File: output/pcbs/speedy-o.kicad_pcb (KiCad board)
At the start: 2 copper layers, 172 x 125.7 mm, 60 parts

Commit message: submit old config
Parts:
- added ?: , HOLE_M2_TH, F.Cu at (135.4, 138.9)
- added ?: , HOLE_M2_TH, F.Cu at (198.4, 141.4)
- added ?: , HOLE_M2_TH, F.Cu at (244.4, 136.3)
- added ?: , HOLE_M2_TH, F.Cu at (105.4, 74.9)
- added ?: , HOLE_M2_TH, F.Cu at (200.4, 57.5)
- added ?: , HOLE_M2_TH, F.Cu at (244.4, 79.3)
- added JST1: , JST_PH_S2B-PH-K_02x2.00mm_Angled, F.Cu at (206.6, 77.4)
- added LED1: , WS2812B,  at (100.9, 154.9)
- added LED10: , WS2812B,  at (135.4, 112.2)
- added LED11: , WS2812B,  at (135.4, 93.2)
- added LED12: , WS2812B,  at (135.4, 74.2)
- added LED13: , WS2812B,  at (154.4, 125.2)
- added LED14: , WS2812B,  at (154.4, 106.2)
- added LED15: , WS2812B,  at (154.4, 87.2)
- added LED16: , WS2812B,  at (154.4, 68.2)
- added LED17: , WS2812B,  at (173.4, 130.9)
- added LED18: , WS2812B,  at (173.4, 111.9)
- added LED19: , WS2812B,  at (173.4, 92.9)
- added LED2: , WS2812B,  at (97.6, 136.2)
- added LED20: , WS2812B,  at (173.4, 73.9)
- added LED21: , WS2812B,  at (192.4, 133.7)
- added LED22: , WS2812B,  at (192.4, 114.7)
- added LED23: , WS2812B,  at (192.4, 95.7)
- added LED24: , WS2812B,  at (192.4, 76.7)
- added LED25: , WS2812B,  at (182.0, 154.7)
- added LED26: , WS2812B,  at (206.5, 160.9)
- added LED27: , WS2812B,  at (213.0, 143.1)
- added LED28: , WS2812B,  at (223.8, 169.3)
- added LED29: , WS2812B,  at (233.3, 152.8)
- added LED3: , WS2812B,  at (94.3, 117.5)
- added LED4: , WS2812B,  at (91.0, 98.8)
- added LED5: , WS2812B,  at (119.6, 151.6)
- added LED6: , WS2812B,  at (116.3, 132.9)
- added LED7: , WS2812B,  at (113.0, 114.2)
- added LED8: , WS2812B,  at (109.7, 95.5)
- added LED9: , WS2812B,  at (135.4, 131.2)
- added TRRS1: TRRS-PJ-320A-dual, TRRS-PJ-320A-dual, F.Cu at (238.4, 73.6)
- D1, D10, D11, D12, D13, D14, D15, D16, D17, D18, D19, D2, D20, D21, D22, D23, D24, D25, D26, D27, D28, D29, D3, D4, D5, D6, D7, D8, D9: value (none) -> Nexperia_CFP3_SOD-123W; footprint ComboDiode -> Diode_SMD:Nexperia_CFP3_SOD-123W; moved to 
- moved D1 11.2 mm to (91.7, 148.4), turned to 100 degrees
- moved D2 11.2 mm to (88.4, 129.7), turned to 100 degrees
- moved D3 11.2 mm to (85.1, 111.0), turned to 100 degrees
- moved D4 11.2 mm to (81.8, 92.3), turned to 100 degrees
- moved D5 11.2 mm to (110.4, 145.1), turned to 100 degrees
- moved D6 11.2 mm to (107.1, 126.4), turned to 100 degrees
- moved D7 11.2 mm to (103.8, 107.7), turned to 100 degrees
- moved D8 11.2 mm to (100.5, 89.0), turned to 100 degrees
- moved D25 11.2 mm to (175.7, 145.4), turned to 80 degrees
- moved D26 11.2 mm to (201.8, 150.7), turned to 70 degrees
- moved D27 11.2 mm to (208.3, 132.8), turned to 70 degrees
- moved D17 11.2 mm to (165.5, 122.9), turned to 90 degrees
- moved D10 11.2 mm to (127.5, 104.2), turned to 90 degrees
- moved D11 11.2 mm to (127.5, 85.2), turned to 90 degrees
- moved D12 11.2 mm to (127.5, 66.2), turned to 90 degrees
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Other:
- board text added: "Speedy-O"

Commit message: update config
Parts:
- removed the ? at (135.4, 138.9)
- removed the ? at (198.4, 141.4)
- removed the ? at (244.4, 136.3)
- removed the ? at (105.4, 74.9)
- removed the ? at (200.4, 57.5)
- removed the ? at (244.4, 79.3)
- removed D28, D29: Nexperia_CFP3_SOD-123W, Diode_SMD:Nexperia_CFP3_SOD-123W
- removed JST1: , JST_PH_S2B-PH-K_02x2.00mm_Angled
- removed LED28, LED29: , WS2812B
- removed MCU1: nice_nano, nice_nano
- removed S28, S29: , PG1350
- added ?: , ProMicro, F.Cu at (207.4, 90.0)
- added T1: , Button_Switch_SMD:SW_SPDT_PCM12, F.Cu at (218.9, 128.0)
- added _2: , Connector_JST:JST_PH_S2B-PH-K_1x02_P2.00mm_Horizontal,  at (209.4, 116.0)
- added _3: , MountingHole_2.2mm_M2_Pad_Via, F.Cu at (120.0, 78.0)
- added _4: , MountingHole_2.2mm_M2_Pad_Via, F.Cu at (134.4, 146.0)
- added _5: , MountingHole_2.2mm_M2_Pad_Via, F.Cu at (170.4, 146.0)
- added _6: , MountingHole_2.2mm_M2_Pad_Via, F.Cu at (213.7, 135.0)
- added _7: , MountingHole_2.2mm_M2_Pad_Via, F.Cu at (220.8, 97.0)
- moved D27 26.8 mm to (219.3, 157.2), turned to 54 degrees
- moved S27 25.0 mm to (226.4, 160.4), turned to -36 degrees
- moved LED27 23.8 mm to (223.5, 164.5), turned to -36 degrees
- moved D16 17.4 mm to (144.8, 77.6)
- moved TRRS1 16.5 mm to (221.9, 74.2)
- moved D15 15.5 mm to (144.8, 94.6)
- moved D20 14.0 mm to (162.8, 79.6)
- moved D14 13.5 mm to (144.8, 111.6)
- moved D24 13.4 mm to (180.8, 81.6)
- moved D12 13.4 mm to (126.8, 79.6)
- moved LED16 12.9 mm to (152.4, 81.0)
- moved S16 12.9 mm to (152.4, 76.0)
- moved D19 12.0 mm to (162.8, 96.6)
- moved D13 11.5 mm to (144.8, 128.6)
- moved D23 11.5 mm to (180.8, 98.6)
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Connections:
- net P006 renamed P10
- net P008 renamed P9
- net P011 renamed P2
- net P017 renamed P8
- net P100 renamed P1
- net P104 renamed P3
- net P106 renamed P4
- net first_home renamed thumb_inner_home
- net index_bottom renamed main_index_bottom
- net index_home renamed main_index_home
- net index_num renamed main_index_num
- net index_top renamed main_index_top
- net inner_bottom renamed main_inner_bottom
- net inner_home renamed main_inner_home
- net inner_num renamed main_inner_num
- net inner_top renamed main_inner_top
- net middle_bottom renamed main_middle_bottom
- net middle_home renamed main_middle_home
- net middle_num renamed main_middle_num
- net middle_top renamed main_middle_top
- net outer_bottom renamed main_outer_bottom
- net outer_home renamed main_outer_home
- net outer_num renamed main_outer_num
- net outer_top renamed main_outer_top
- net pinky_bottom renamed main_pinky_bottom
- net pinky_home renamed main_pinky_home
- net pinky_num renamed main_pinky_num
- net pinky_top renamed main_pinky_top
- net ring_bottom renamed main_ring_bottom
- net ring_home renamed main_ring_home
- net ring_num renamed main_ring_num
- net ring_top renamed main_ring_top
- net second_home renamed thumb_home_home
- net second_upper renamed thumb_outer_home
- D25 pad 1: (no net) -> P11
- D26 pad 1: (no net) -> P11
- D27 pad 1: (no net) -> P11
- LED1 pad 4: (no net) -> rgb_main_outer_bottom
- LED10 pad 2: (no net) -> rgb_main_ring_bottom
- LED10 pad 4: (no net) -> rgb_main_ring_home
- LED11 pad 2: (no net) -> rgb_main_ring_home
- LED11 pad 4: (no net) -> rgb_main_ring_top
- LED12 pad 2: (no net) -> rgb_main_ring_top
- LED12 pad 4: (no net) -> rgb_main_ring_num
- LED13 pad 2: (no net) -> rgb_main_middle_home
- LED13 pad 4: (no net) -> rgb_main_middle_bottom
- LED14 pad 2: (no net) -> rgb_main_middle_top
- LED14 pad 4: (no net) -> rgb_main_middle_home
- LED15 pad 2: (no net) -> rgb_main_middle_num
- LED15 pad 4: (no net) -> rgb_main_middle_top
- LED16 pad 2: (no net) -> rgb_main_ring_num
- LED16 pad 4: (no net) -> rgb_main_middle_num
- LED17 pad 2: (no net) -> rgb_thumb_home_home
- LED17 pad 4: (no net) -> rgb_main_index_bottom
- LED18 pad 2: (no net) -> rgb_main_index_bottom
- LED18 pad 4: (no net) -> rgb_main_index_home
- LED19 pad 2: (no net) -> rgb_main_index_home
- LED19 pad 4: (no net) -> rgb_main_index_top
- LED2 pad 2: (no net) -> rgb_main_outer_bottom
- LED2 pad 4: (no net) -> rgb_main_outer_home
- LED20 pad 2: (no net) -> rgb_main_index_top
- LED20 pad 4: (no net) -> rgb_main_index_num
- LED21 pad 2: (no net) -> rgb_main_inner_home
- LED21 pad 4: (no net) -> rgb_main_inner_bottom
- LED22 pad 2: (no net) -> rgb_main_inner_top
- LED22 pad 4: (no net) -> rgb_main_inner_home
- LED23 pad 2: (no net) -> rgb_main_inner_num
- LED23 pad 4: (no net) -> rgb_main_inner_top
- LED24 pad 2: (no net) -> rgb_main_index_num
- LED24 pad 4: (no net) -> rgb_main_inner_num
- LED25 pad 2: (no net) -> rgb_main_middle_bottom
- LED25 pad 4: (no net) -> rgb_thumb_inner_home
- LED26 pad 2: (no net) -> rgb_thumb_inner_home
- LED26 pad 4: (no net) -> rgb_thumb_home_home
- LED27 pad 2: (no net) -> rgb_main_inner_bottom
- LED27 pad 4: (no net) -> P12
- LED3 pad 2: (no net) -> rgb_main_outer_home
- LED3 pad 4: (no net) -> rgb_main_outer_top
- LED4 pad 2: (no net) -> rgb_main_outer_top
- LED4 pad 4: (no net) -> rgb_main_outer_num
- LED5 pad 2: (no net) -> rgb_main_pinky_home
- LED5 pad 4: (no net) -> rgb_main_pinky_bottom
- LED6 pad 2: (no net) -> rgb_main_pinky_top
- LED6 pad 4: (no net) -> rgb_main_pinky_home
- LED7 pad 2: (no net) -> rgb_main_pinky_num
- LED7 pad 4: (no net) -> rgb_main_pinky_top
- LED8 pad 2: (no net) -> rgb_main_outer_num
- LED8 pad 4: (no net) -> rgb_main_pinky_num
- LED9 pad 2: (no net) -> rgb_main_pinky_bottom
- LED9 pad 4: (no net) -> rgb_main_ring_bottom
- S13 pad 1: P020 -> P7
- S14 pad 1: P020 -> P7
- S15 pad 1: P020 -> P7
- S16 pad 1: P020 -> P7
- S17 pad 1: P022 -> P6
- S18 pad 1: P022 -> P6
- S19 pad 1: P022 -> P6
- S20 pad 1: P022 -> P6
- S21 pad 1: P024 -> P5
- S22 pad 1: P024 -> P5
- S23 pad 1: P024 -> P5
- S24 pad 1: P024 -> P5
- S25 pad 1: P009 -> P5
- S26 pad 1: P010 -> P6
- S27 pad 1: P111 -> P7
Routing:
- net (no net): track 0.00 -> 371.4 mm
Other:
- board size 172 x 125.7 mm -> 159.3 x 108.6 mm
- board text added: "Speedy-O v0.1.0"
- board text removed: "Speedy-O"

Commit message: alternative layout
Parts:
- moved TRRS1 46.7 mm to (218.1, 120.8), turned to -90 degrees
- moved _2 10.2 mm to (199.2, 116.0), turned to 180 degrees
- moved T1 2.24 mm to (216.7, 128.0)
- moved ? 1.00 mm to (208.4, 90.0)
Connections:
- D25 pad 1: P11 -> P8
- D25 pad 2: thumb_inner_home -> thumb_outer_home
- D26 pad 1: P11 -> P8
- D27 pad 1: P11 -> P8
- D27 pad 2: thumb_outer_home -> thumb_inner_home
- LED25 pad 4: rgb_thumb_inner_home -> rgb_thumb_outer_home
- LED27 pad 4: P12 -> P9
- S25 pad 2: thumb_inner_home -> thumb_outer_home
- S26 pad 1: P6 -> P4
- S27 pad 1: P7 -> P3
- S27 pad 2: thumb_outer_home -> thumb_inner_home
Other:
- outline, holes or cut-outs redrawn

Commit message: update routing
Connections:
- D1 pad 1: P1 -> P6
- D10 pad 1: P2 -> P7
- D11 pad 1: P3 -> P8
- D12 pad 1: P4 -> P9
- D13 pad 1: P1 -> P6
- D14 pad 1: P2 -> P7
- D15 pad 1: P3 -> P8
- D16 pad 1: P4 -> P9
- D17 pad 1: P1 -> P6
- D18 pad 1: P2 -> P7
- D19 pad 1: P3 -> P8
- D2 pad 1: P2 -> P7
- D20 pad 1: P4 -> P9
- D21 pad 1: P1 -> P6
- D22 pad 1: P2 -> P7
- D23 pad 1: P3 -> P8
- D24 pad 1: P4 -> P9
- D25 pad 1: P8 -> P16
- D26 pad 1: P8 -> P16
- D27 pad 1: P8 -> P16
- D3 pad 1: P3 -> P8
- D4 pad 1: P4 -> P9
- D5 pad 1: P1 -> P6
- D6 pad 1: P2 -> P7
- D7 pad 1: P3 -> P8
- D8 pad 1: P4 -> P9
- D9 pad 1: P1 -> P6
- LED1 pad 2: (no net) -> rgb_main_outer_home
- LED10 pad 2: rgb_main_ring_bottom -> rgb_main_pinky_top
- LED11 pad 2: rgb_main_ring_home -> rgb_main_middle_top
- LED12 pad 2: rgb_main_ring_top -> (no net)
- LED13 pad 2: rgb_main_middle_home -> rgb_main_index_bottom
- LED14 pad 2: rgb_main_middle_top -> rgb_main_ring_home
- LED15 pad 2: rgb_main_middle_num -> rgb_main_index_top
- LED17 pad 2: rgb_thumb_home_home -> rgb_main_inner_bottom
- LED18 pad 2: rgb_main_index_bottom -> rgb_main_middle_home
- LED19 pad 2: rgb_main_index_home -> rgb_main_inner_top
- LED2 pad 2: rgb_main_outer_bottom -> rgb_main_pinky_home
- LED20 pad 2: rgb_main_index_top -> rgb_main_middle_num
- LED22 pad 2: rgb_main_inner_top -> rgb_main_index_home
- LED25 pad 2: rgb_main_middle_bottom -> rgb_main_pinky_bottom
- LED26 pad 2: rgb_thumb_inner_home -> rgb_thumb_outer_home
- LED27 pad 2: rgb_main_inner_bottom -> rgb_thumb_home_home
- LED3 pad 2: rgb_main_outer_home -> rgb_main_outer_num
- LED4 pad 2: rgb_main_outer_top -> rgb_main_pinky_num
- LED5 pad 2: rgb_main_pinky_home -> rgb_main_outer_bottom
- LED6 pad 2: rgb_main_pinky_top -> rgb_main_ring_bottom
- LED7 pad 2: rgb_main_pinky_num -> rgb_main_outer_top
- LED8 pad 2: rgb_main_outer_num -> rgb_main_ring_top
- LED9 pad 2: rgb_main_pinky_bottom -> rgb_main_middle_bottom
- S1 pad 1: P10 -> P3
- S10 pad 1: P8 -> P5
- S11 pad 1: P8 -> P5
- S12 pad 1: P8 -> P5
- S13 pad 1: P7 -> P18
- S14 pad 1: P7 -> P18
- S15 pad 1: P7 -> P18
- S16 pad 1: P7 -> P18
- S17 pad 1: P6 -> P15
- S18 pad 1: P6 -> P15
- S19 pad 1: P6 -> P15
- S2 pad 1: P10 -> P3
- S20 pad 1: P6 -> P15
- S21 pad 1: P5 -> P14
- S22 pad 1: P5 -> P14
- S23 pad 1: P5 -> P14
- S24 pad 1: P5 -> P14
- S25 pad 1: P5 -> P18
- S26 pad 1: P4 -> P15
- S27 pad 1: P3 -> P14
- S3 pad 1: P10 -> P3
- S4 pad 1: P10 -> P3
- S5 pad 1: P9 -> P4
- S6 pad 1: P9 -> P4
- S7 pad 1: P9 -> P4
- S8 pad 1: P9 -> P4
- S9 pad 1: P8 -> P5
- TRRS1 pad 4: P0 -> P10

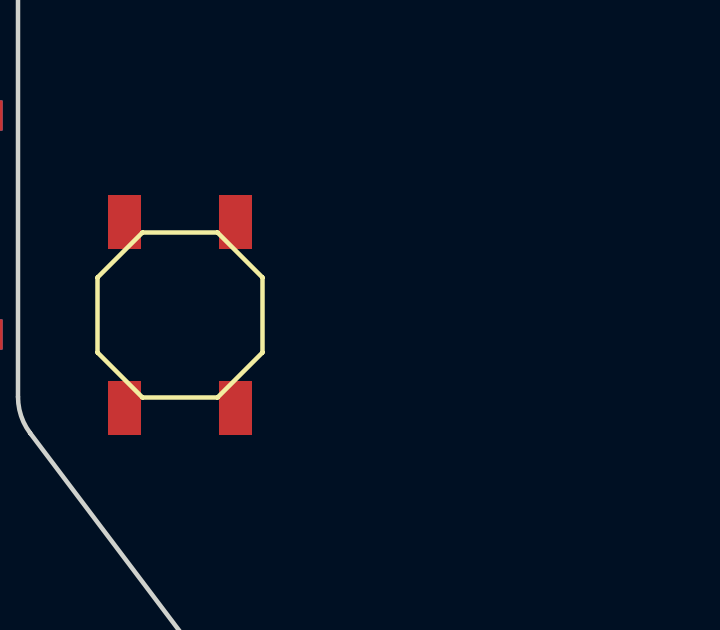
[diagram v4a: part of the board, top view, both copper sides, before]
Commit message: add reset button on the back
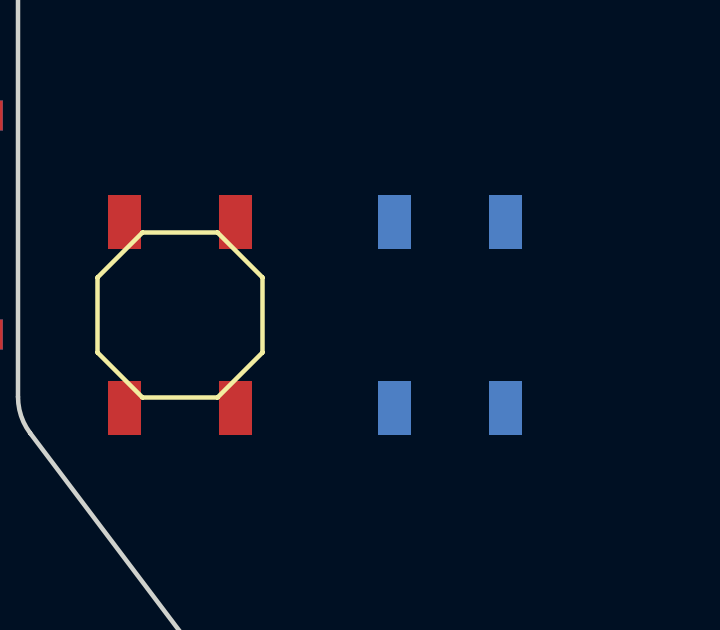
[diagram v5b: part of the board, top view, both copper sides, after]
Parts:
- added B2: , E73:SW_TACT_ALPS_SKQGABE010, F.Cu at (233.4, 131.0)
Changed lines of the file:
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@@
         (pad 2 smd rect (at 3.1 1.85 -90) (size 1.8 1.1) (layers F.Cu F.Paste F.Mask) (net 77 "RST"))
+    )
+    (module E73:SW_TACT_ALPS_SKQGABE010 (layer F.Cu)
+        (descr "Low-profile SMD Tactile Switch, https://www.e-switch.com/product-catalog/tact/product-lines/tl3342-series-low-profile-smt-tact-switch")
+        (tags "SPST Tactile Switch")
+        (at 233.4131489 131.0063062 -90)
+        (fp_text reference "B2" (at 0 0) (layer F.SilkS) hide (effects (font (size 1.27 1.27) (thickness 0.15))))
+        (fp_text value "" (at 0 0) (layer F.SilkS) hide (effects (font (size 1.27 1.27) (thickness 0.15))))
+        (fp_line (start 2.75 1.25) (end 1.25 2.75) (layer B.SilkS) (width 0.15))
+        (fp_line (start 2.75 -1.25) (end 1.25 -2.75) (layer B.SilkS) (width 0.15))
+        (fp_line (start 2.75 -1.25) (end 2.75 1.25) (layer B.SilkS) (width 0.15))
+        (fp_line (start -1.25 2.75) (end 1.25 2.75) (layer B.SilkS) (width 0.15))
+        (fp_line (start -1.25 -2.75) (end 1.25 -2.75) (layer B.SilkS) (width 0.15))
+        (fp_line (start -2.75 1.25) (end -1.25 2.75) (layer B.SilkS) (width 0.15))
+        (fp_line (start -2.75 -1.25) (end -1.25 -2.75) (layer B.SilkS) (width 0.15))
+        (fp_line (start -2.75 -1.25) (end -2.75 1.25) (layer B.SilkS) (width 0.15))
+        (pad 1 smd rect (at -3.1 -1.85 -90) (size 1.8 1.1) (layers B.Cu B.Paste B.Mask) (net 4 "GND"))
+        (pad 1 smd rect (at 3.1 -1.85 -90) (size 1.8 1.1) (layers B.Cu B.Paste B.Mask) (net 4 "GND"))
+        (pad 2 smd rect (at -3.1 1.85 -90) (size 1.8 1.1) (layers B.Cu B.Paste B.Mask) (net 77 "RST"))
+        (pad 2 smd rect (at 3.1 1.85 -90) (size 1.8 1.1) (layers B.Cu B.Paste B.Mask) (net 77 "RST"))
     )
       (module TRRS-PJ-320A-dual (layer F.Cu)

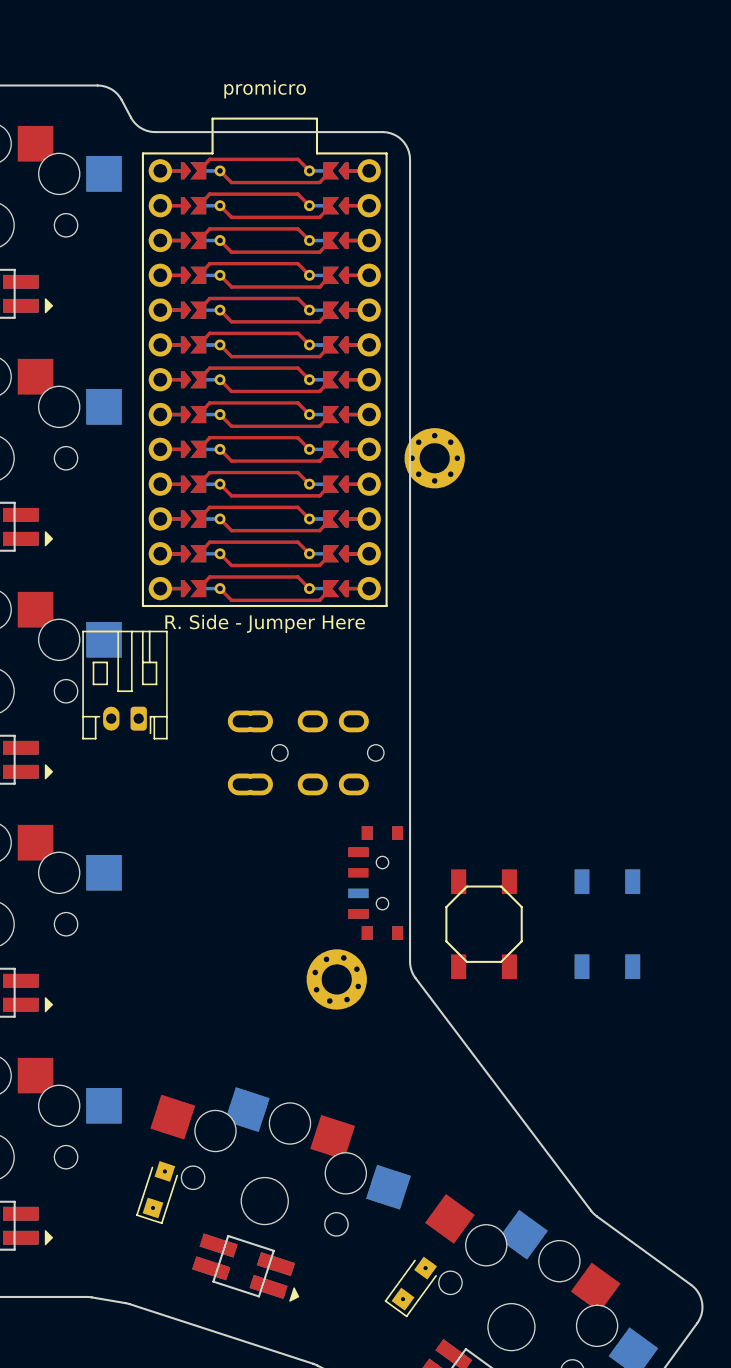
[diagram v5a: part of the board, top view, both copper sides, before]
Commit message: update position of components
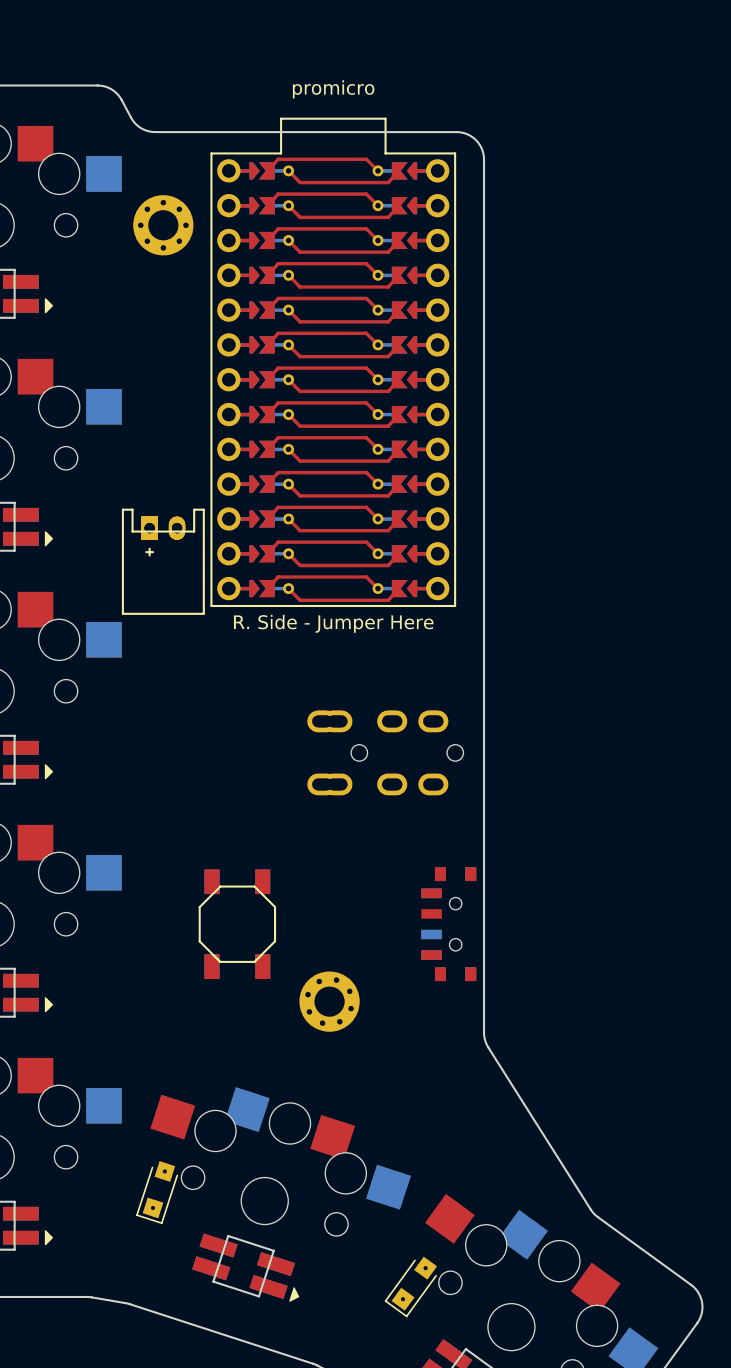
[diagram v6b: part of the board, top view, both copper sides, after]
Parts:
- removed _7: , MountingHole_2.2mm_M2_Pad_Via
- added JST1, JST2: , JST_PH_S2B-PH-K_02x2.00mm_Angled, F.Cu at (201.0, 102.1)
- _2: footprint Connector_JST:JST_PH_S2B-PH-K_1x02_P2.00mm_Horizontal -> MountingHole_2.2mm_M2_Pad_Via; moved to F.Cu
- moved _2 87.8 mm to (120.0, 78.0), turned to 0 degrees
- moved _3 69.5 mm to (134.4, 146.0)
- moved _6 56.5 mm to (201.0, 80.0), turned to 0 degrees
- moved _5 43.7 mm to (213.1, 136.7), turned to -18 degrees
- moved _4 36.0 mm to (170.4, 146.0)
- moved B2 27.0 mm to (206.4, 131.0)
- moved B1 18.0 mm to (206.4, 131.0)
- moved T1 6.12 mm to (222.0, 131.0)
- moved TRRS1 5.80 mm to (223.9, 120.8)
- moved ? 5.00 mm to (213.4, 90.0)
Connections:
- _2 pad 1: pos -> (no net)
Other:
- outline, holes or cut-outs redrawn
